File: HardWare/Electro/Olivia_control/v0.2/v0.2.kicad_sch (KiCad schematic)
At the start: 47 parts, among them J1 PROG, J10 Motor_B, J11 I2C, J12 DAC, J13 UART2, J15 TRIAC_220VAC, J17 In12V, J2 Input1, J3 Input2, J4 Input3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

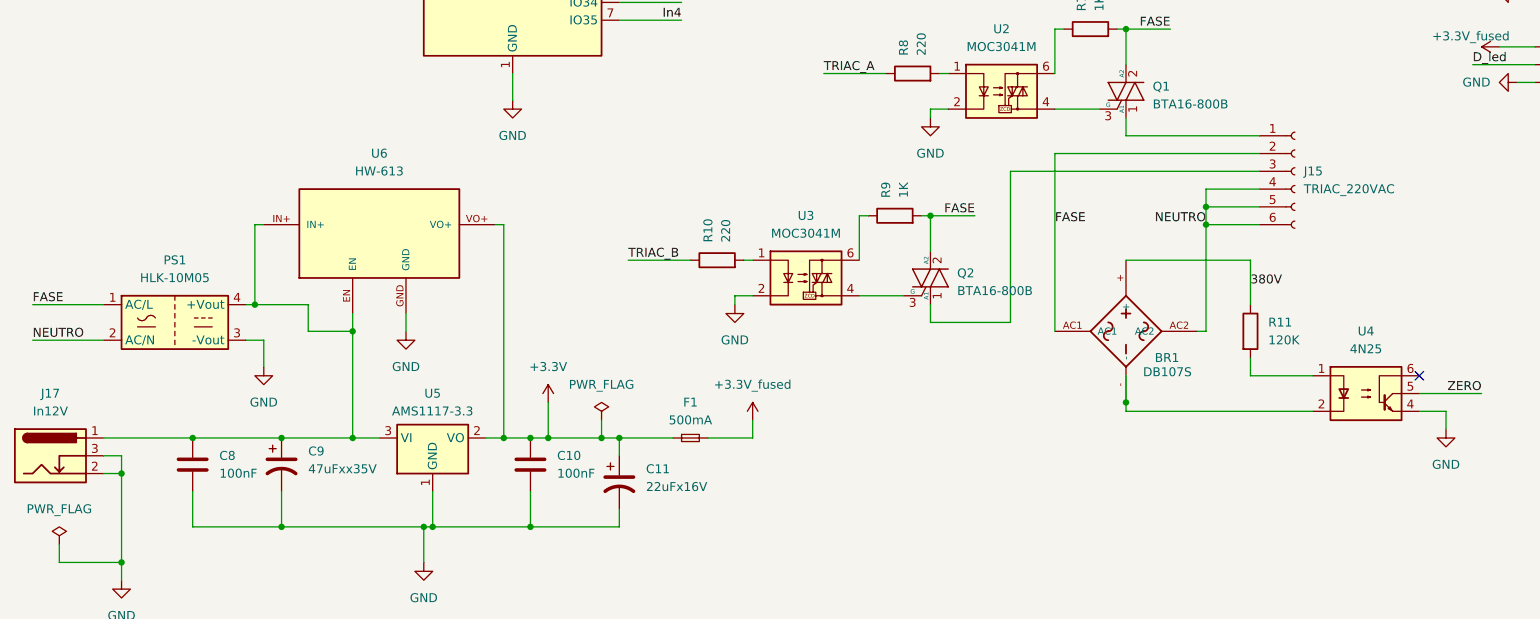
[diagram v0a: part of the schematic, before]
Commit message: Reemplazo de Conector 220V por borneras 7,62mm.
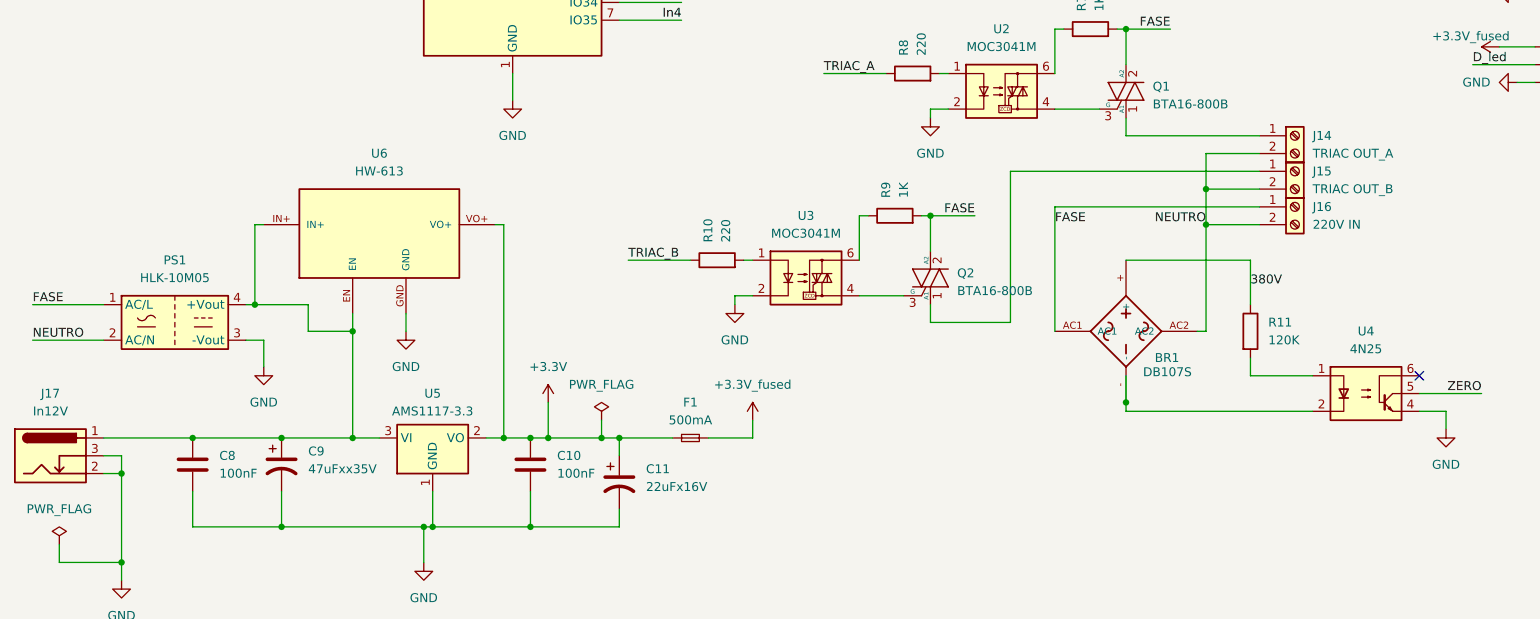
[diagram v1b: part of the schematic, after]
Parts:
- removed J15: TRIAC_220VAC, lib:Molex_Mini-Fit_Jr_5569-06A2_2x03_P4.20mm_Horizontal_NoHoles, symbol Connector:Conn_01x06_Socket
- added J14: TRIAC OUT_A, Connector_Phoenix_GMSTB:PhoenixContact_GMSTBA_2,5_2-G-7,62_1x02_P7.62mm_Horizontal, symbol Connector:Screw_Terminal_01x02
- added J15: TRIAC OUT_B, Connector_Phoenix_GMSTB:PhoenixContact_GMSTBA_2,5_2-G-7,62_1x02_P7.62mm_Horizontal, symbol Connector:Screw_Terminal_01x02
- added J16: 220V IN, Connector_Phoenix_GMSTB:PhoenixContact_GMSTBA_2,5_2-G-7,62_1x02_P7.62mm_Horizontal, symbol Connector:Screw_Terminal_01x02
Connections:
- net FASE: now also J16.1 (Pin_1)
- net NEUTRO: now also J14.2 (Pin_2), J15.2 (Pin_2), J16.2 (Pin_2)
- net at Q2.1 (A1): now also J15.1 (Pin_1)
- net at Q1.1 (A1): now also J14.1 (Pin_1)
